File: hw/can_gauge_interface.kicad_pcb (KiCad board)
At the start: 4 copper layers, 75 x 75 mm, 61 parts, among them J1 Conn_02x04_Top_Bottom, J2 Analog, J3 Power debug, J4 Power debug, J5 SPI debug, J6 I^{2}C debug, J7 CAN debug, J8 SWD, U1 STM32C092CBT6, U2 TPS5430DDA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

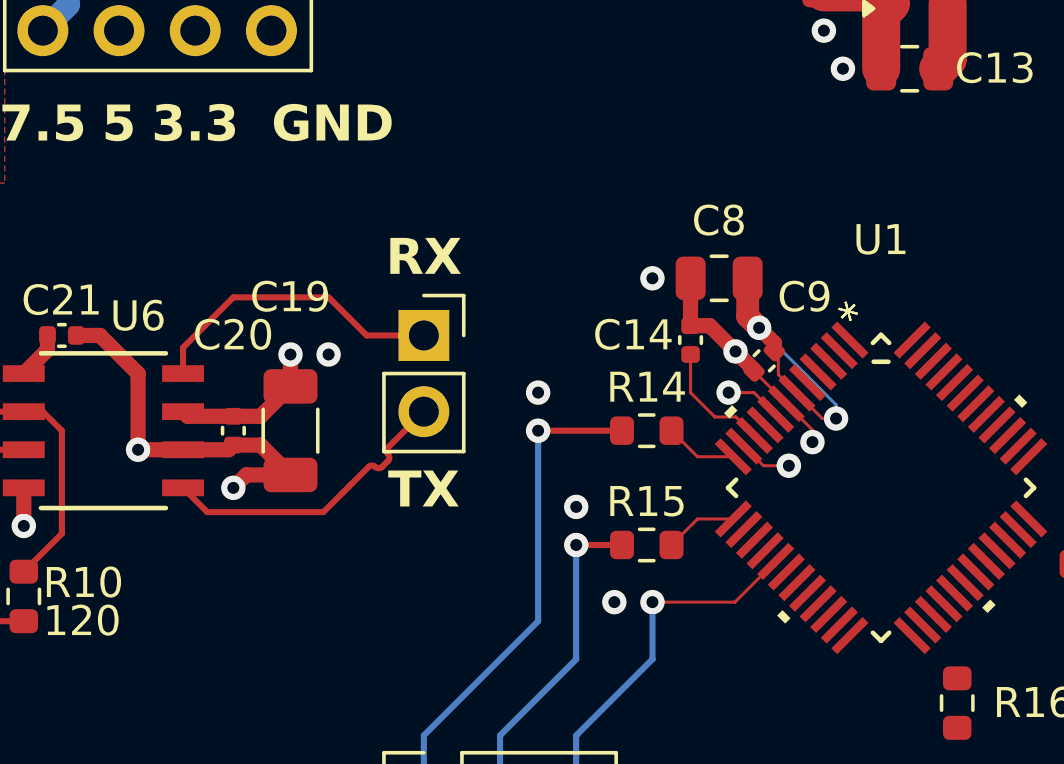
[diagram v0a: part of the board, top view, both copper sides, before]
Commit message: pcb: CAN routing
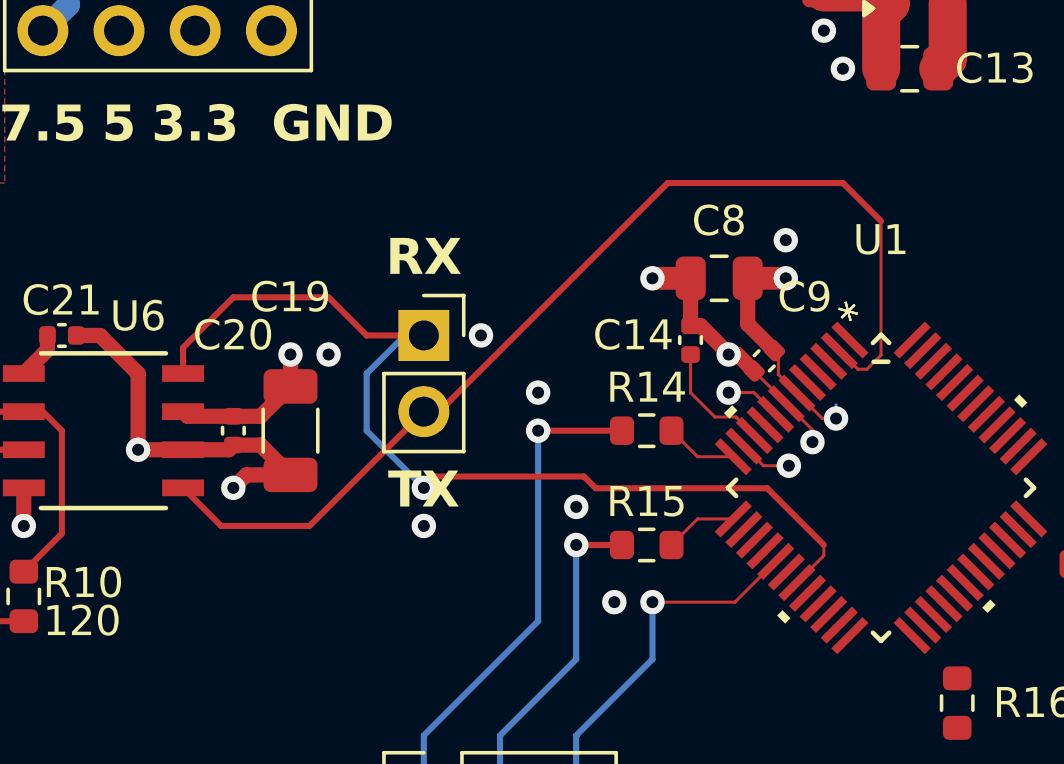
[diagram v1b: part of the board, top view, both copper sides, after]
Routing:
- net CAN_TX: track 10.1 -> 35.4 mm
- net CAN_RX: track 10.1 -> 33.2 mm, vias 0 -> 1
- net +3.3V: track 14.1 -> 11.8 mm
- net GND: track 44.9 -> 46.2 mm, vias 40 -> 43

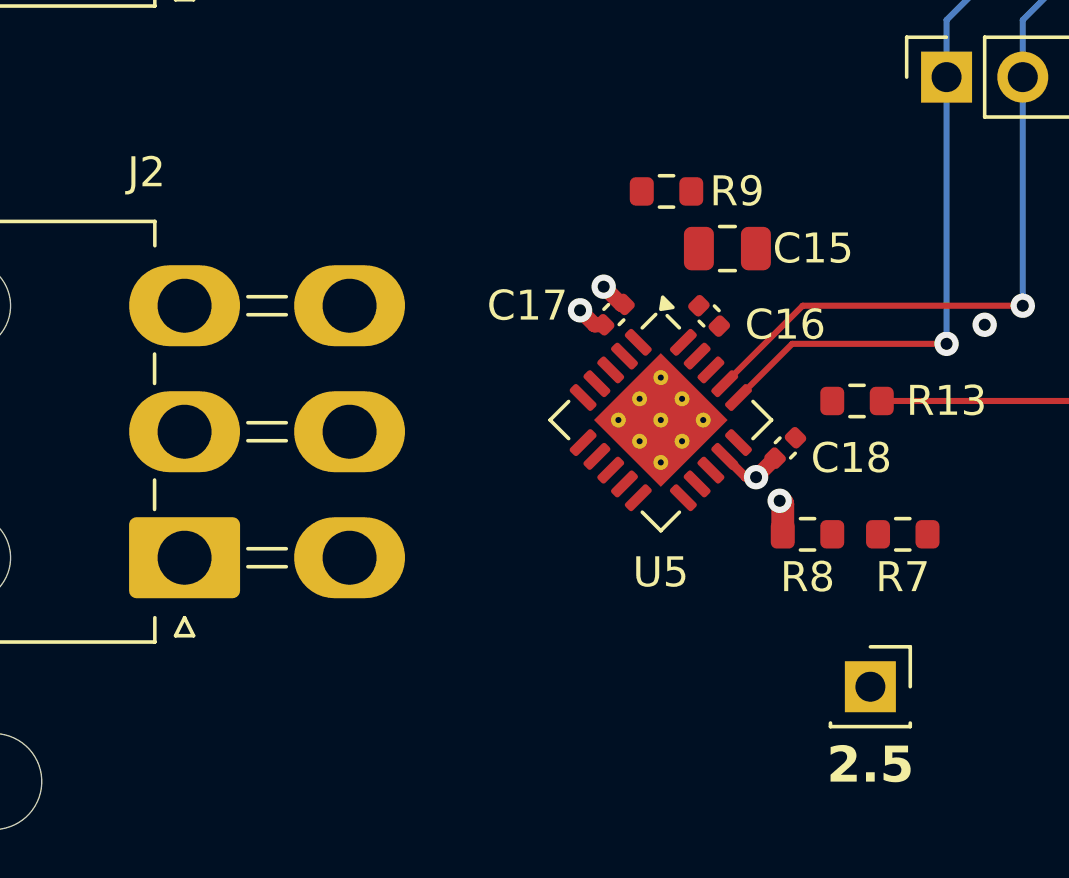
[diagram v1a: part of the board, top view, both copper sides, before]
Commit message: pcb: dac routing
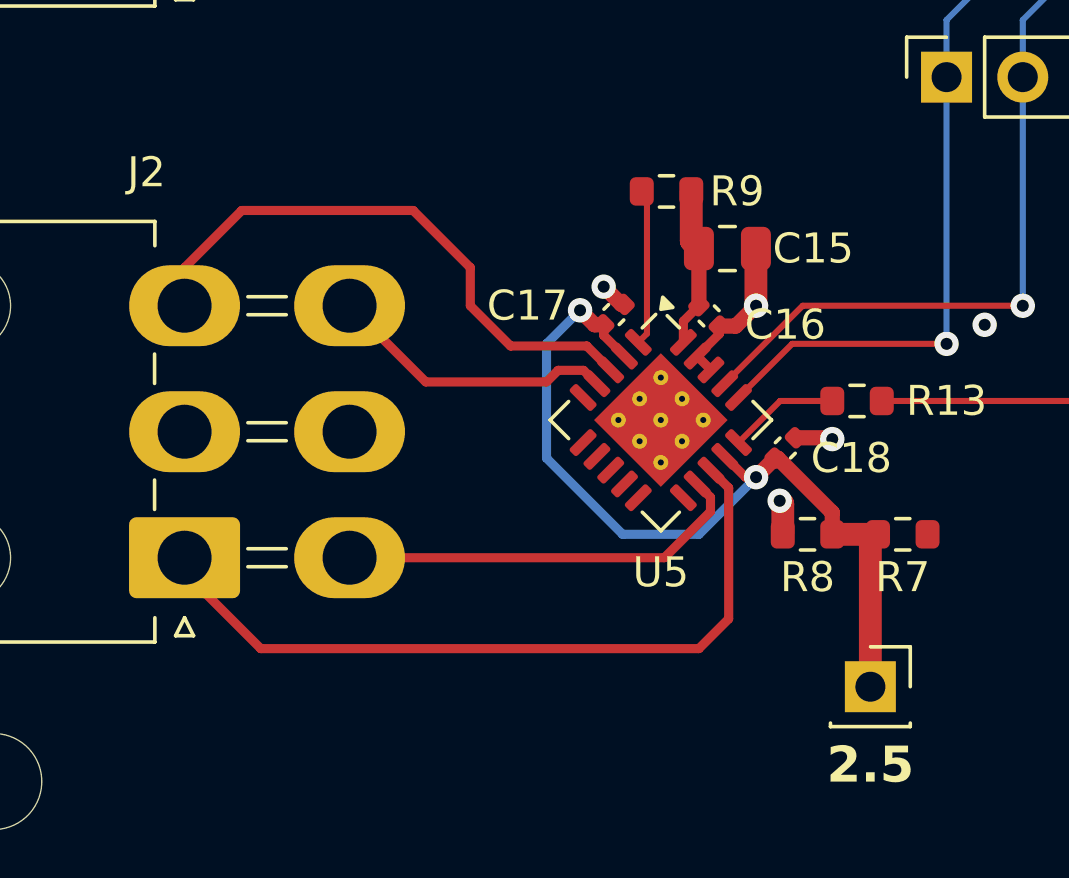
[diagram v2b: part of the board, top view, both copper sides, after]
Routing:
- net +2.5V: track 3.22 -> 28.8 mm
- net An2: track 0.00 -> 25.3 mm
- net An1: track 0.00 -> 19.2 mm
- net An4: track 0.00 -> 13.8 mm
- net An3: track 0.00 -> 9.64 mm
- net GND: track 46.2 -> 52.8 mm, vias 43 -> 45
- net +3.3V: track 11.8 -> 17.1 mm
- net DAC_~{CS}: track 0.00 -> 5.22 mm
- net /DAC_SDO: track 0.00 -> 3.70 mm

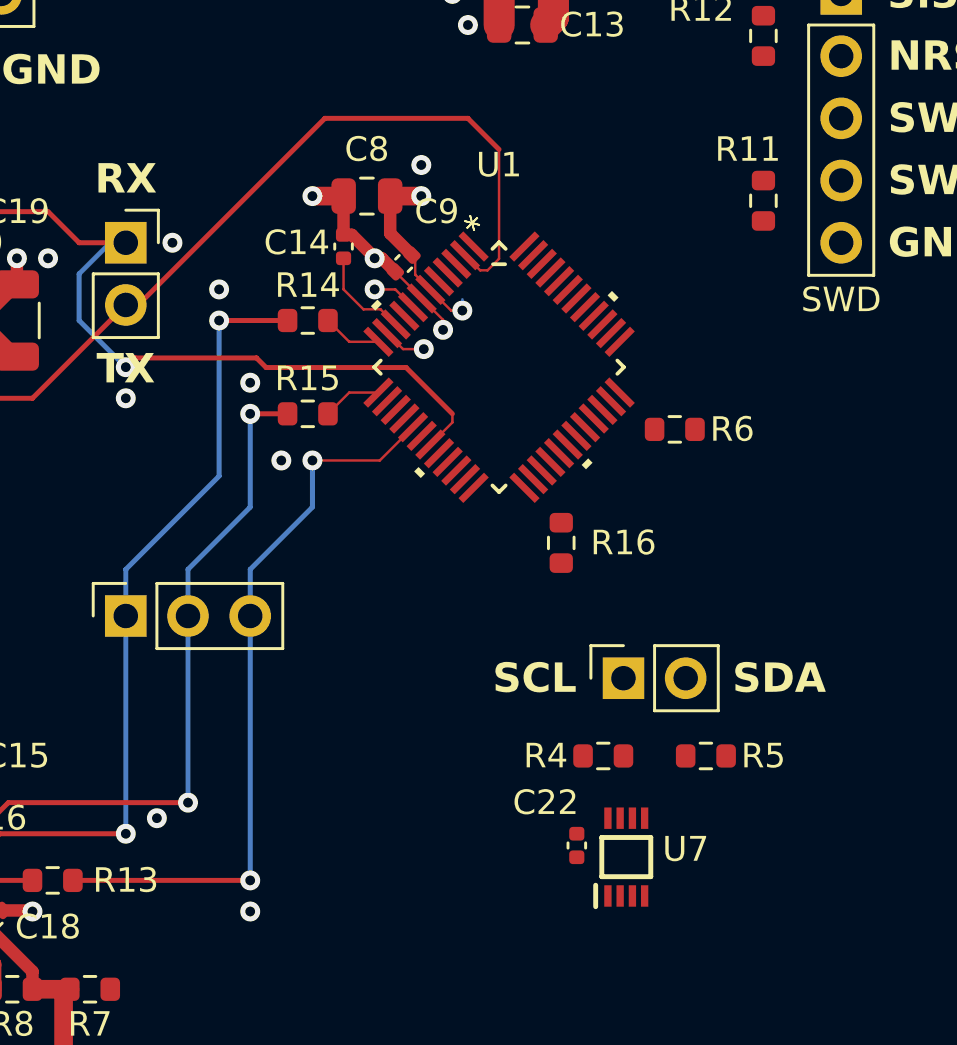
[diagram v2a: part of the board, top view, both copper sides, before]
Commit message: pcb: eeprom routing
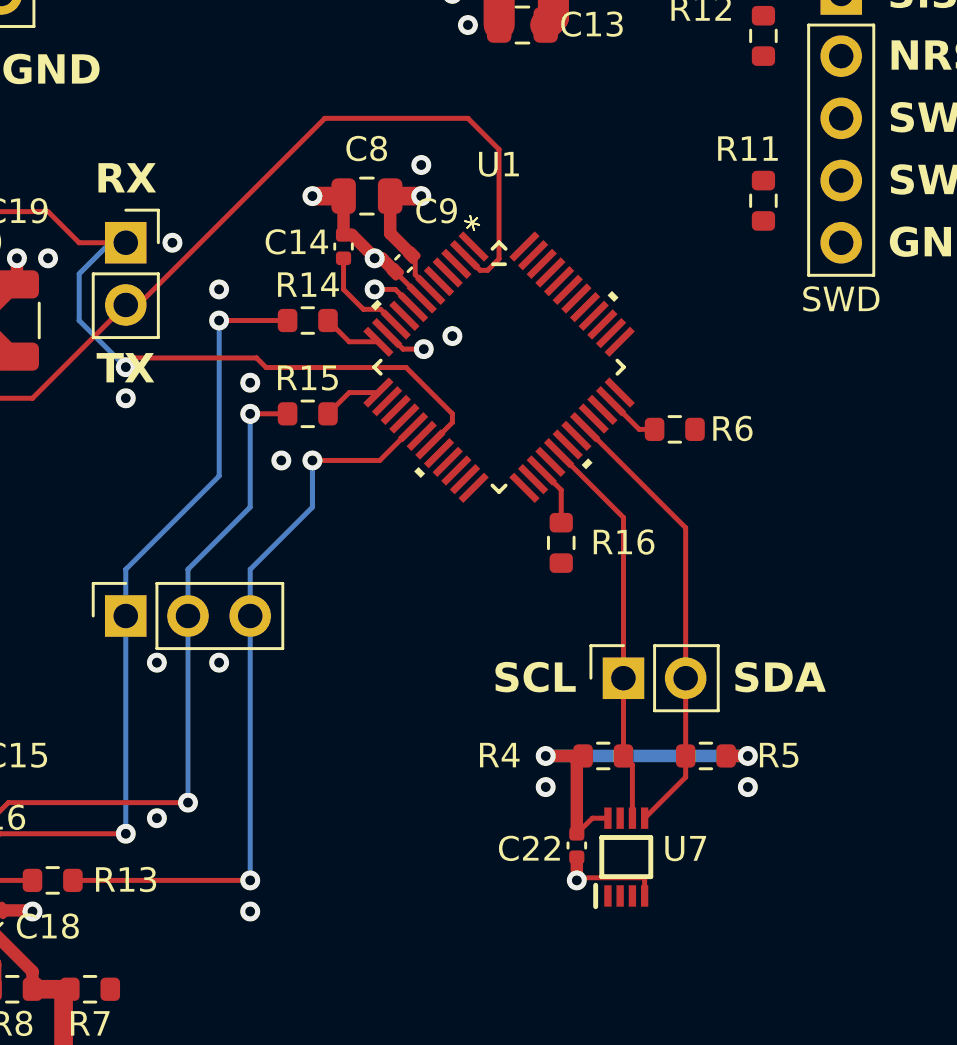
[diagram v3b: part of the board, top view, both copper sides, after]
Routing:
- net I2C_SDA: track 0.00 -> 18.4 mm
- net I2C_SCL: track 0.00 -> 16.1 mm
- net +3.3V: track 17.1 -> 30.5 mm, vias 2 -> 3
- net GND: track 52.8 -> 55.6 mm, vias 45 -> 50
- net /DAC_~{CS}_R: track 0.00 -> 2.46 mm
- net /SWDIO_R: track 0.00 -> 2.25 mm

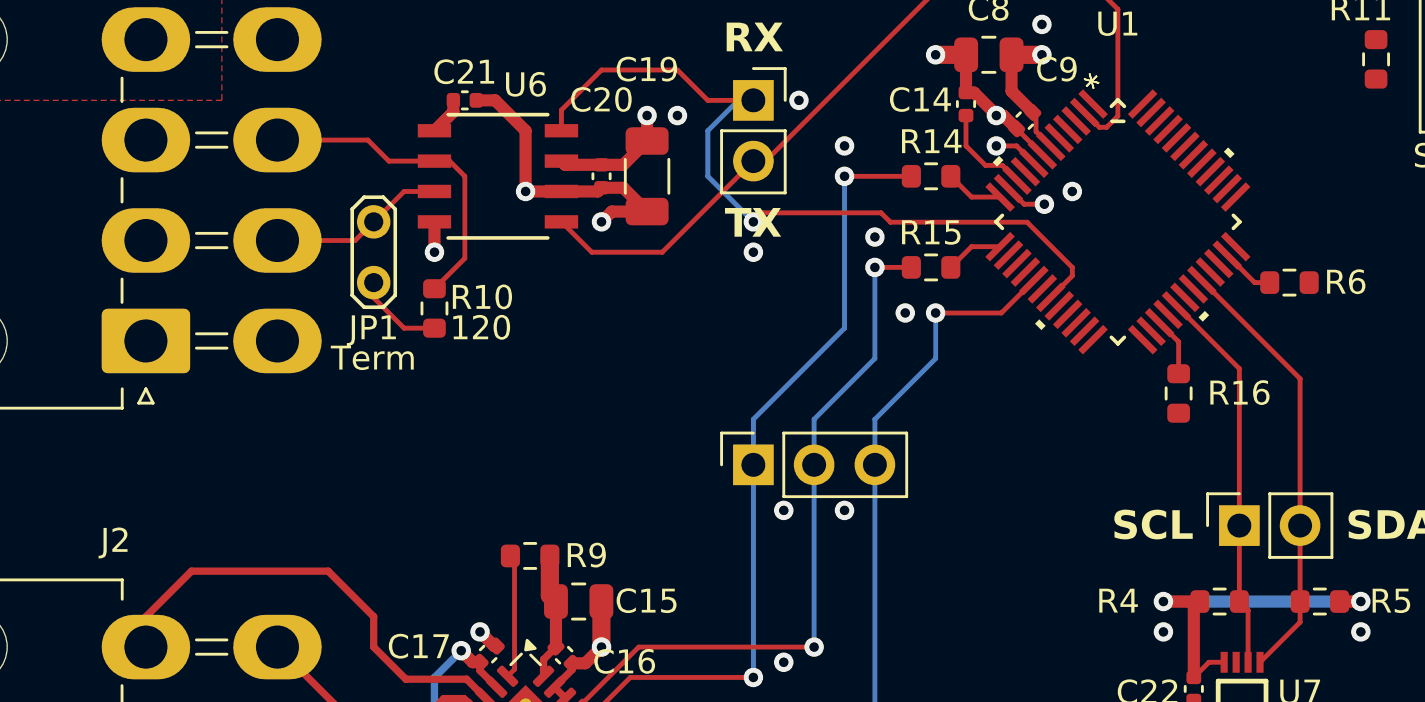
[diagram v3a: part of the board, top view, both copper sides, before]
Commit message: pcb: signal routing
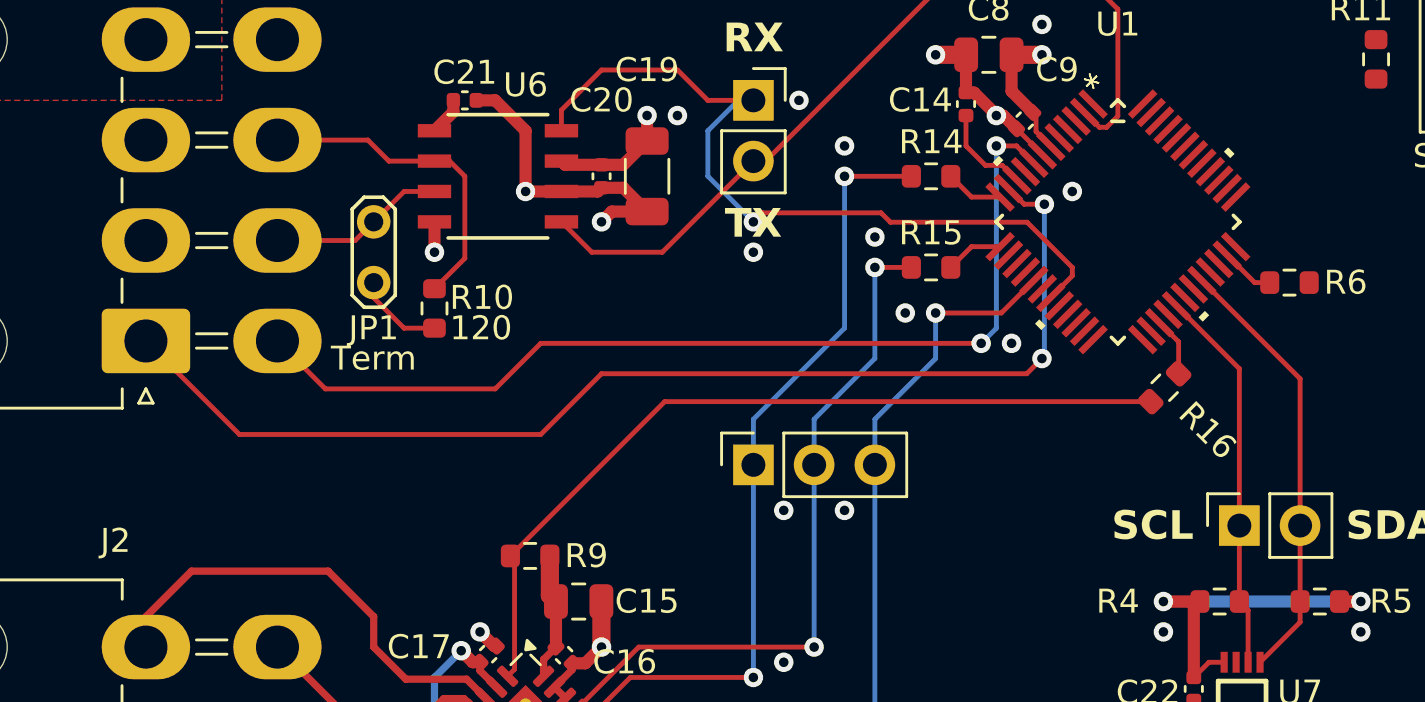
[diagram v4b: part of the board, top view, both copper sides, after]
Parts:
- moved R16 0.63 mm to (129.0, 93.3), turned to 45 degrees
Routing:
- net Tach: track 1.77 -> 48.7 mm, vias 1 -> 2
- net Speed: track 1.87 -> 41.4 mm, vias 1 -> 2
- net DAC_~{CS}: track 5.22 -> 34.7 mm
- net GND: vias 50 -> 51
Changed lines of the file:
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@@
 	(footprint "Resistor_SMD:R_0603_1608Metric"
 		(layer "F.Cu")
-		(at 129.54 93.535 90)
+		(at 128.956637 93.293363 45)
 		(descr "Resistor SMD 0603 (1608 Metric), square (rectangular) end terminal, IPC_7351 nominal, (Body size source: IPC-SM-782 page 72, https://www.pcb-3d.com/wordpress/wp-content/uploads/ipc-sm-782a_amendment_1_and_2.pdf), generated with kicad-footprint-generator")
 		(tags "resistor")
 		(property "Reference" "R16"
-			(at 0 2.54 180)
+			(at 0 2.54 135)
 			(layer "F.SilkS")
 			(effects
@@
 		)
 		(property "Value" "22"
-			(at 0 1.43 90)
+			(at 0 1.43 45)
 			(layer "F.Fab")
 			(hide yes)
@@
 		)
 		(property "Datasheet" ""
-			(at 0 0 90)
+			(at 0 0 45)
 			(unlocked yes)
 			(layer "F.Fab")
@@
 		)
 		(property "Description" "Resistor, US symbol"
-			(at 0 0 90)
+			(at 0 0 45)
 			(unlocked yes)
 			(layer "F.Fab")
@@
 		)
 		(fp_line
-			(start 1.48 -0.73)
-			(end 1.48 0.73)
+			(start -1.48 -0.73)
+			(end 1.48 -0.73)
 			(stroke
 				(width 0.05)
@@
 		)
 		(fp_line
-			(start -1.48 -0.73)
-			(end 1.48 -0.73)
+			(start -1.48 0.73)
+			(end -1.48 -0.73)
 			(stroke
 				(width 0.05)
@@
 		)
 		(fp_line
-			(start 1.48 0.73)
-			(end -1.48 0.73)
+			(start 1.48 -0.73)
+			(end 1.48 0.73)
 			(stroke
 				(width 0.05)
@@
 		)
 		(fp_line
-			(start -1.48 0.73)
-			(end -1.48 -0.73)
+			(start 1.48 0.73)
+			(end -1.48 0.73)
 			(stroke
 				(width 0.05)
@@
 		)
 		(fp_line
-			(start 0.8 -0.4125)
-			(end 0.8 0.4125)
+			(start -0.8 -0.4125)
+			(end 0.8 -0.4125)
 			(stroke
 				(width 0.1)
@@
 		)
 		(fp_line
-			(start -0.8 -0.4125)
-			(end 0.8 -0.4125)
+			(start -0.8 0.4125)
+			(end -0.8 -0.4125)
 			(stroke
 				(width 0.1)
@@
 		)
 		(fp_line
-			(start 0.8 0.4125)
-			(end -0.8 0.4125)
+			(start 0.8 -0.4125)
+			(end 0.8 0.4125)
 			(stroke
 				(width 0.1)
@@
 		)
 		(fp_line
-			(start -0.8 0.4125)
-			(end -0.8 -0.4125)
+			(start 0.8 0.4125)
+			(end -0.8 0.4125)
 			(stroke
 				(width 0.1)
@@
 		)
 		(fp_text user "${REFERENCE}"
-			(at 0 0 90)
+			(at 0 0 45)
 			(layer "F.Fab")
 			(effects
@@
 		)
 		(pad "1" smd roundrect
-			(at -0.825 0 90)
+			(at -0.825 0 45)
 			(size 0.8 0.95)
 			(layers "F.Cu" "F.Mask" "F.Paste")
@@
 		)
 		(pad "2" smd roundrect
-			(at 0.825 0 90)
+			(at 0.825 0 45)
 			(size 0.8 0.95)
 			(layers "F.Cu" "F.Mask" "F.Paste")
@@
 	)
 	(via
+		(at 122.555 91.44)
+		(size 0.8128)
+		(drill 0.4)
+		(layers "F.Cu" "B.Cu")
+		(free yes)
+		(net 1)
+	)
+	(via
 		(at 127 66.04)
 		(size 0.8128)
@@
 	)
 	(segment
+		(start 121.285 91.44)
+		(end 102.87 91.44)
+		(width 0.2032)
+		(layer "F.Cu")
+		(net 10)
+	)
+	(segment
+		(start 102.87 91.44)
+		(end 100.965 93.345)
+		(width 0.2032)
+		(layer "F.Cu")
+		(net 10)
+	)
+	(segment
+		(start 93.865 93.345)
+		(end 91.86 91.34)
+		(width 0.2032)
+		(layer "F.Cu")
+		(net 10)
+	)
+	(segment
+		(start 100.965 93.345)
+		(end 93.865 93.345)
+		(width 0.2032)
+		(layer "F.Cu")
+		(net 10)
+	)
+	(segment
 		(start 123.488224 83.908886)
 		(end 122.764338 83.185)
@@
 	)
 	(via
+		(at 121.285 91.44)
+		(size 0.8128)
+		(drill 0.4)
+		(layers "F.Cu" "B.Cu")
+		(net 10)
+	)
+	(via
 		(at 121.92 83.185)
 		(size 0.8128)
@@
 	)
 	(segment
+		(start 121.92 83.185)
+		(end 121.92 90.805)
+		(width 0.2032)
+		(layer "B.Cu")
+		(net 10)
+	)
+	(segment
+		(start 121.92 90.805)
+		(end 121.285 91.44)
+		(width 0.2032)
+		(layer "B.Cu")
+		(net 10)
+	)
+	(segment
+		(start 90.27 95.25)
+		(end 86.36 91.34)
+		(width 0.2032)
+		(layer "F.Cu")
+		(net 11)
+	)
+	(segment
+		(start 123.19 92.71)
+		(end 105.41 92.71)
+		(width 0.2032)
+		(layer "F.Cu")
+		(net 11)
+	)
+	(segment
+		(start 123.825 92.075)
+		(end 123.19 92.71)
+		(width 0.2032)
+		(layer "F.Cu")
+		(net 11)
+	)
+	(segment
 		(start 122.427564 84.969546)
 		(end 123.080888 85.62287)
@@
 	)
 	(segment
+		(start 102.87 95.25)
+		(end 90.27 95.25)
+		(width 0.2032)
+		(layer "F.Cu")
+		(net 11)
+	)
+	(segment
 		(start 123.080888 85.62287)
 		(end 123.92713 85.62287)
@@
 		(net 11)
 	)
+	(segment
+		(start 105.41 92.71)
+		(end 102.87 95.25)
+		(width 0.2032)
+		(layer "F.Cu")
+		(net 11)
+	)
+	(via
+		(at 123.825 92.075)
+		(size 0.8128)
+		(drill 0.4)
+		(layers "F.Cu" "B.Cu")
+		(net 11)
+	)
 	(via
 		(at 123.92713 85.62287)
@@
 	)
 	(segment
+		(start 123.92713 91.97287)
+		(end 123.825 92.075)
+		(width 0.2032)
+		(layer "B.Cu")
+		(net 11)
+	)
+	(segment
+		(start 123.92713 85.62287)
+		(end 123.92713 91.97287)
+		(width 0.2032)
+		(layer "B.Cu")
+		(net 11)
+	)
+	(segment
 		(start 97.155 85.09)
 		(end 95.885 86.36)
@@
 		(width 0.2032)
 		(layer "F.Cu")
+		(net 59)
+	)
+	(segment
+		(start 108.053274 93.876726)
+		(end 101.6 100.33)
+		(width 0.2032)
+		(layer "F.Cu")
+		(net 59)
+	)
+	(segment
+		(start 128.373274 93.876726)
+		(end 108.053274 93.876726)
+		(width 0.2032)
+		(layer "F.Cu")
